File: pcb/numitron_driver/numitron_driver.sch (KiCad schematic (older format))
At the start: 4 parts, among them J0 Conn_01x08_Male, J1 IV-9, U0 TPIC6595

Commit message: driver v1.0
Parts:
- C0: value 100nF -> 0.1uF
- J0: value Conn_01x08_Male -> Conn_02x04_Male; footprint (none) -> Connector_PinHeader_2.54mm:PinHeader_2x04_P2.54mm_Vertical; symbol Connector:Conn_01x08_Male -> Connector_Generic_MountingPin:Conn_02x04_Odd_Even_MountingPin
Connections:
- wire segments 40 -> 34
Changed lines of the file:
@@
 EESchema Schematic File Version 4
+LIBS:numitron_driver-cache
 EELAYER 30 0
 EELAYER END
@@
 	4150 2450 3950 2450
 $Comp
-L power:GND #PWR?
+L power:GND #PWR0101
 U 1 1 5D91C224
 P 3150 2950
-F 0 "#PWR?" H 3150 2700 50  0001 C CNN
+F 0 "#PWR0101" H 3150 2700 50  0001 C CNN
 F 1 "GND" H 3300 2850 50  0000 C CNN
 F 2 "" H 3150 2950 50  0001 C CNN
@@
 $EndComp
 $Comp
-L Connector:Conn_01x08_Male J0
+L Connector_Generic_MountingPin:Conn_02x04_Odd_Even_MountingPin J0
 U 1 1 5D91CB5D
-P 1850 2000
-F 0 "J0" H 1958 2481 50  0000 C CNN
-F 1 "Conn_01x08_Male" H 1958 2390 50  0000 C CNN
-F 2 "" H 1850 2000 50  0001 C CNN
-F 3 "~" H 1850 2000 50  0001 C CNN
-	1    1850 2000
+P 1850 1950
+F 0 "J0" H 1850 2250 50  0000 C CNN
+F 1 "Conn_02x04_Male" H 2150 2150 50  0000 C CNN
+F 2 "Connector_PinHeader_2.54mm:PinHeader_2x04_P2.54mm_Vertical" H 1850 1950 50  0001 C CNN
+F 3 "~" H 1850 1950 50  0001 C CNN
+	1    1850 1950
 	1    0    0    -1
 $EndComp
-Wire Wire Line
-	2050 1700 2550 1700
-Wire Wire Line
-	2550 1700 2550 1300
 $Comp
 L Device:C C0
@@
 P 2700 1450
 F 0 "C0" H 2815 1496 50  0000 L CNN
-F 1 "100nF" H 2815 1405 50  0000 L CNN
+F 1 "0.1uF" H 2815 1405 50  0000 L CNN
 F 2 "Capacitor_SMD:C_0805_2012Metric_Pad1.15x1.40mm_HandSolder" H 2738 1300 50  0001 C CNN
 F 3 "~" H 2700 1450 50  0001 C CNN
@@
 Wire Wire Line
 	3450 1300 4150 1300
-Wire Wire Line
-	2950 1750 2850 1750
-Wire Wire Line
-	2850 1750 2850 1900
-Wire Wire Line
-	2050 1900 2850 1900
-Wire Wire Line
-	2950 1950 2850 1950
-Wire Wire Line
-	2850 1950 2850 2000
-Wire Wire Line
-	2050 2000 2850 2000
-Wire Wire Line
-	2950 2050 2850 2050
-Wire Wire Line
-	2850 2050 2850 2100
-Wire Wire Line
-	2050 2100 2850 2100
-Wire Wire Line
-	2850 2200 2850 2250
-Wire Wire Line
-	2850 2250 2950 2250
-Wire Wire Line
-	2050 2200 2850 2200
-Wire Wire Line
-	2050 2300 2850 2300
-Wire Wire Line
-	2850 2300 2850 2350
-Wire Wire Line
-	2850 2350 2950 2350
 Connection ~ 2700 1300
 Wire Wire Line
-	2700 1300 2550 1300
-Wire Wire Line
 	2700 1300 3450 1300
-Wire Wire Line
-	2700 1600 2700 1800
-Wire Wire Line
-	2700 1800 2050 1800
-Wire Wire Line
-	2700 1800 2700 2950
-Connection ~ 2700 1800
 Wire Wire Line
 	2700 2950 3150 2950
@@
 	3950 2650 3950 3150
 Wire Wire Line
-	3950 3150 2050 3150
+	3950 3150 2150 3150
 Wire Wire Line
-	2050 3150 2050 2400
+	1650 1300 2700 1300
+Wire Wire Line
+	2700 1600 2700 1850
+Wire Wire Line
+	2150 2150 2150 3150
+Wire Wire Line
+	2150 1850 2700 1850
+Connection ~ 2700 1850
+Wire Wire Line
+	2700 1850 2700 2950
+Wire Wire Line
+	2150 1950 2950 1950
+Wire Wire Line
+	2150 2050 2950 2050
+Wire Wire Line
+	1650 1850 1650 1300
+Wire Wire Line
+	2950 1750 1550 1750
+Wire Wire Line
+	1550 1750 1550 1950
+Wire Wire Line
+	1550 1950 1650 1950
+Wire Wire Line
+	1650 2250 1650 2150
+Wire Wire Line
+	1650 2250 2950 2250
+Wire Wire Line
+	1650 2050 1550 2050
+Wire Wire Line
+	1550 2050 1550 2350
+Wire Wire Line
+	1550 2350 2950 2350
 $EndSCHEMATC

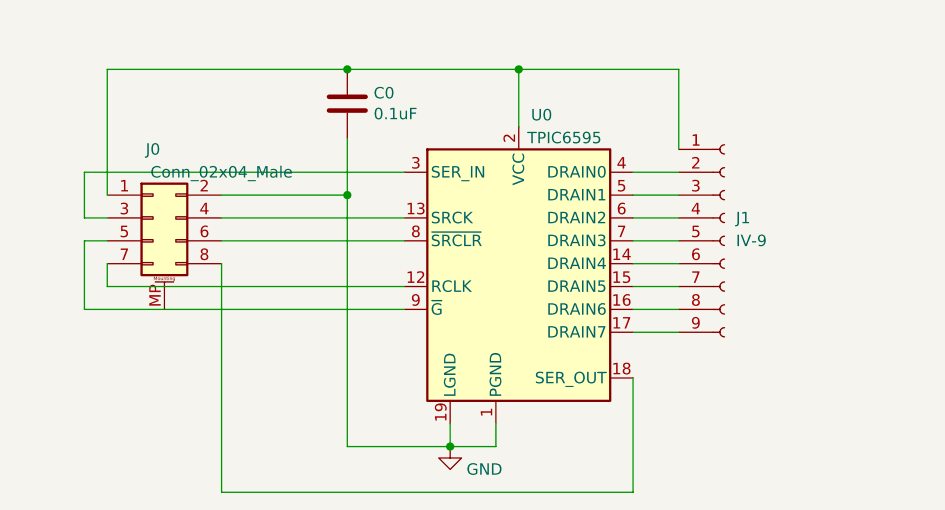
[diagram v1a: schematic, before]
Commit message: driver and basic shiftout test code for the tube driver
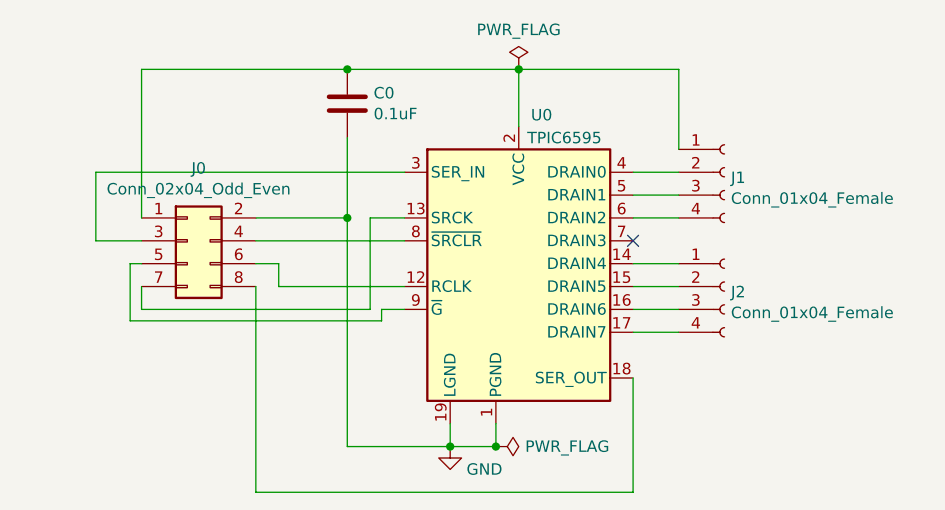
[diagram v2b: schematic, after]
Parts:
- removed J0: Conn_02x04_Male, Connector_PinHeader_2.54mm:PinHeader_2x04_P2.54mm_Vertical, symbol Connector_Generic_MountingPin:Conn_02x04_Odd_Even_MountingPin
- removed J1: IV-9, numitron_clock:NUM_IV-9, symbol Connector:Conn_01x09_Female
- added J0: Conn_02x04_Odd_Even, Connector_PinSocket_2.54mm:PinSocket_2x04_P2.54mm_Vertical, symbol Connector_Generic:Conn_02x04_Odd_Even
- added J1, J2: Conn_01x04_Female, Connector_PinHeader_2.54mm:PinHeader_1x04_P2.54mm_Vertical, symbol Connector:Conn_01x04_Female
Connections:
- net GND: now also J0.2 (Pin_2)
- net at U0.12 (RCLK): now also J0.6 (Pin_6)
- net at U0.13 (SRCK): now also J0.7 (Pin_7)
- net at U0.14 (DRAIN4): now also J2.1 (Pin_1)
- net at U0.15 (DRAIN5): now also J2.2 (Pin_2)
- net at U0.16 (DRAIN6): now also J2.3 (Pin_3)
- net at U0.17 (DRAIN7): now also J2.4 (Pin_4)
- net at U0.18 (SER_OUT): now also J0.8 (Pin_8)
- net at C0.1, U0.2 (VCC): now also J0.1 (Pin_1), J1.1 (Pin_1)
- net at U0.3 (SER_IN): now also J0.3 (Pin_3)
- net at U0.4 (DRAIN0): now also J1.2 (Pin_2)
- net at U0.5 (DRAIN1): now also J1.3 (Pin_3)
- net at U0.6 (DRAIN2): now also J1.4 (Pin_4)
- net at U0.8 (~SRCLR): now also J0.4 (Pin_4)
- net at U0.9 (~G): now also J0.5 (Pin_5)
- no-connect marks 0 -> 1
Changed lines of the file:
@@
 EESchema Schematic File Version 4
-LIBS:numitron_driver-cache
 EELAYER 30 0
 EELAYER END
@@
 Wire Wire Line
 	3350 2850 3350 2950
-$Comp
-L Connector:Conn_01x09_Female J1
-U 1 1 5D8DB2C8
-P 4350 2050
-F 0 "J1" H 4400 2150 50  0000 L CNN
-F 1 "IV-9" H 4400 2050 50  0000 L CNN
-F 2 "numitron_clock:NUM_IV-9" H 4350 2050 50  0001 C CNN
-F 3 "~" H 4350 2050 50  0001 C CNN
-	1    4350 2050
-	1    0    0    -1
-$EndComp
 Wire Wire Line
 	4150 1650 4150 1300
-Wire Wire Line
-	4150 1750 3950 1750
-Wire Wire Line
-	4150 1850 3950 1850
-Wire Wire Line
-	4150 1950 3950 1950
-Wire Wire Line
-	4150 2050 3950 2050
-Wire Wire Line
-	4150 2150 3950 2150
-Wire Wire Line
-	4150 2250 3950 2250
-Wire Wire Line
-	4150 2350 3950 2350
-Wire Wire Line
-	4150 2450 3950 2450
 $Comp
 L power:GND #PWR0101
@@
 F 3 "" H 3150 2950 50  0001 C CNN
 	1    3150 2950
-	1    0    0    -1
-$EndComp
-$Comp
-L Connector_Generic_MountingPin:Conn_02x04_Odd_Even_MountingPin J0
-U 1 1 5D91CB5D
-P 1850 1950
-F 0 "J0" H 1850 2250 50  0000 C CNN
-F 1 "Conn_02x04_Male" H 2150 2150 50  0000 C CNN
-F 2 "Connector_PinHeader_2.54mm:PinHeader_2x04_P2.54mm_Vertical" H 1850 1950 50  0001 C CNN
-F 3 "~" H 1850 1950 50  0001 C CNN
-	1    1850 1950
 	1    0    0    -1
 $EndComp
@@
 Wire Wire Line
 	3450 1300 4150 1300
-Connection ~ 2700 1300
 Wire Wire Line
 	2700 1300 3450 1300
@@
 	3950 2650 3950 3150
 Wire Wire Line
-	3950 3150 2150 3150
+	2700 1600 2700 1950
+$Comp
+L Connector:Conn_01x04_Female J1
+U 1 1 5EA7DC0D
+P 4350 1750
+F 0 "J1" H 4378 1726 50  0000 L CNN
+F 1 "Conn_01x04_Female" H 4378 1635 50  0000 L CNN
+F 2 "Connector_PinHeader_2.54mm:PinHeader_1x04_P2.54mm_Vertical" H 4350 1750 50  0001 C CNN
+F 3 "~" H 4350 1750 50  0001 C CNN
+	1    4350 1750
+	1    0    0    -1
+$EndComp
+$Comp
+L Connector:Conn_01x04_Female J2
+U 1 1 5EA7E475
+P 4350 2250
+F 0 "J2" H 4378 2226 50  0000 L CNN
+F 1 "Conn_01x04_Female" H 4378 2135 50  0000 L CNN
+F 2 "Connector_PinHeader_2.54mm:PinHeader_1x04_P2.54mm_Vertical" H 4350 2250 50  0001 C CNN
+F 3 "~" H 4350 2250 50  0001 C CNN
+	1    4350 2250
+	1    0    0    -1
+$EndComp
 Wire Wire Line
-	1650 1300 2700 1300
+	4150 2350 3950 2350
 Wire Wire Line
-	2700 1600 2700 1850
+	4150 2250 3950 2250
 Wire Wire Line
-	2150 2150 2150 3150
+	4150 2150 3950 2150
 Wire Wire Line
-	2150 1850 2700 1850
-Connection ~ 2700 1850
+	4150 1950 3950 1950
 Wire Wire Line
-	2700 1850 2700 2950
+	4150 1850 3950 1850
 Wire Wire Line
-	2150 1950 2950 1950
+	4150 1750 3950 1750
+$Comp
+L Connector_Generic:Conn_02x04_Odd_Even J0
+U 1 1 5EA831DC
+P 2000 2050
+F 0 "J0" H 2050 2367 50  0000 C CNN
+F 1 "Conn_02x04_Odd_Even" H 2050 2276 50  0000 C CNN
+F 2 "Connector_PinSocket_2.54mm:PinSocket_2x04_P2.54mm_Vertical" H 2000 2050 50  0001 C CNN
+F 3 "~" H 2000 2050 50  0001 C CNN
+	1    2000 2050
+	1    0    0    -1
+$EndComp
 Wire Wire Line
-	2150 2050 2950 2050
+	1800 1950 1800 1300
 Wire Wire Line
-	1650 1850 1650 1300
+	1800 1300 2700 1300
+Connection ~ 2700 1300
 Wire Wire Line
-	2950 1750 1550 1750
+	2300 1950 2700 1950
+Connection ~ 2700 1950
 Wire Wire Line
-	1550 1750 1550 1950
+	2700 1950 2700 2950
 Wire Wire Line
-	1550 1950 1650 1950
+	1800 2050 1600 2050
 Wire Wire Line
-	1650 2250 1650 2150
+	1600 2050 1600 1750
 Wire Wire Line
-	1650 2250 2950 2250
+	1600 1750 2950 1750
 Wire Wire Line
-	1650 2050 1550 2050
+	2300 2250 2300 3150
 Wire Wire Line
-	1550 2050 1550 2350
+	2300 3150 3950 3150
 Wire Wire Line
-	1550 2350 2950 2350
+	1800 2250 1800 2350
+$Comp
+L power:PWR_FLAG #FLG0101
+U 1 1 5EA87197
+P 3450 1300
+F 0 "#FLG0101" H 3450 1375 50  0001 C CNN
+F 1 "PWR_FLAG" H 3450 1473 50  0000 C CNN
+F 2 "" H 3450 1300 50  0001 C CNN
+F 3 "~" H 3450 1300 50  0001 C CNN
+	1    3450 1300
+	1    0    0    -1
+$EndComp
+$Comp
+L power:PWR_FLAG #FLG0102
+U 1 1 5EA87DBB
+P 3350 2950
+F 0 "#FLG0102" H 3350 3025 50  0001 C CNN
+F 1 "PWR_FLAG" V 3350 3078 50  0000 L CNN
+F 2 "" H 3350 2950 50  0001 C CNN
+F 3 "~" H 3350 2950 50  0001 C CNN
+	1    3350 2950
+	0    1    1    0
+$EndComp
+Connection ~ 3350 2950
+Wire Wire Line
+	2850 2350 2950 2350
+Wire Wire Line
+	2800 1950 2800 2350
+Wire Wire Line
+	2800 2350 1800 2350
+Wire Wire Line
+	2800 1950 2950 1950
+Wire Wire Line
+	2950 2250 2400 2250
+Wire Wire Line
+	2400 2250 2400 2150
+Wire Wire Line
+	2400 2150 2300 2150
+Wire Wire Line
+	3950 2450 4150 2450
+NoConn ~ 3950 2050
+Wire Wire Line
+	2300 2050 2950 2050
+Wire Wire Line
+	2850 2350 2850 2400
+Wire Wire Line
+	2850 2400 1750 2400
+Wire Wire Line
+	1750 2400 1750 2150
+Wire Wire Line
+	1750 2150 1800 2150
 $EndSCHEMATC
